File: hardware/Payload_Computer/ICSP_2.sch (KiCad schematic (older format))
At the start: 3 parts

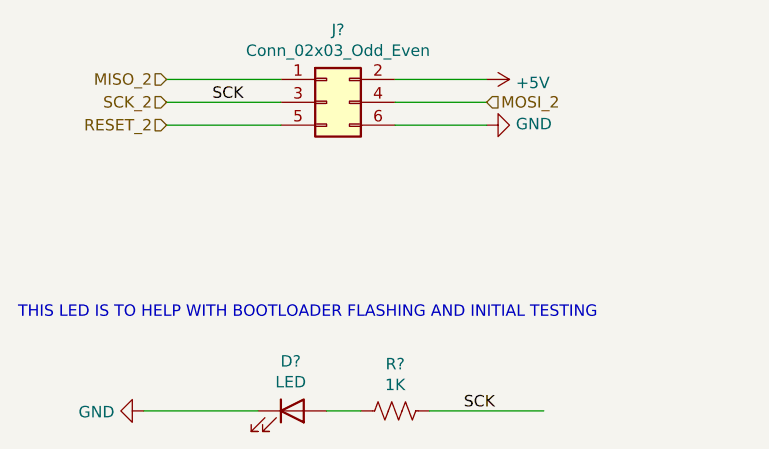
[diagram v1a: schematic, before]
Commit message: Finished BNO055
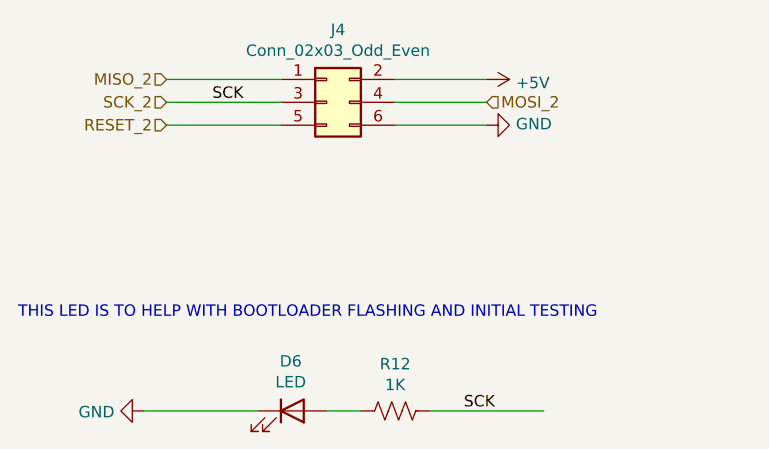
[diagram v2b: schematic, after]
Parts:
- gave numbers to parts that had none: 3
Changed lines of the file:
@@
 $Descr A4 11693 8268
 encoding utf-8
-Sheet 11 17
+Sheet 11 15
 Title ""
 Date ""
@@
 $EndDescr
 $Comp
-L Connector_Generic:Conn_02x03_Odd_Even J?
+L Connector_Generic:Conn_02x03_Odd_Even J4
 U 1 1 5F8F4559
 P 6000 3950
-F 0 "J?" H 6050 4267 50  0000 C CNN
+F 0 "J4" H 6050 4267 50  0000 C CNN
 F 1 "Conn_02x03_Odd_Even" H 6050 4176 50  0000 C CNN
 F 2 "" H 6000 3950 50  0001 C CNN
@@
 P 5850 5300
 AR Path="/5F8F06D7/5F988B3F" Ref="D?"  Part="1"
-AR Path="/5F8F071C/5F988B3F" Ref="D?"  Part="1"
-F 0 "D?" H 5843 5517 50  0000 C CNN
+AR Path="/5F8F071C/5F988B3F" Ref="D6"  Part="1"
+F 0 "D6" H 5843 5517 50  0000 C CNN
 F 1 "LED" H 5843 5426 50  0000 C CNN
 F 2 "" H 5850 5300 50  0001 C CNN
@@
 P 6300 5300
 AR Path="/5F8F06D7/5F988B45" Ref="R?"  Part="1"
-AR Path="/5F8F071C/5F988B45" Ref="R?"  Part="1"
-F 0 "R?" V 6095 5300 50  0000 C CNN
+AR Path="/5F8F071C/5F988B45" Ref="R12"  Part="1"
+F 0 "R12" V 6095 5300 50  0000 C CNN
 F 1 "1K" V 6186 5300 50  0000 C CNN
 F 2 "" V 6340 5290 50  0001 C CNN
@@
 P 5200 5300
 AR Path="/5F8F06D7/5F988B4B" Ref="#PWR?"  Part="1"
-AR Path="/5F8F071C/5F988B4B" Ref="#PWR?"  Part="1"
-F 0 "#PWR?" H 5200 5050 50  0001 C CNN
+AR Path="/5F8F071C/5F988B4B" Ref="#PWR0138"  Part="1"
+F 0 "#PWR0138" H 5200 5050 50  0001 C CNN
 F 1 "GND" V 5205 5172 50  0000 R CNN
 F 2 "" H 5200 5300 50  0001 C CNN
